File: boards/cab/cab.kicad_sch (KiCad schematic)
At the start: 0 parts

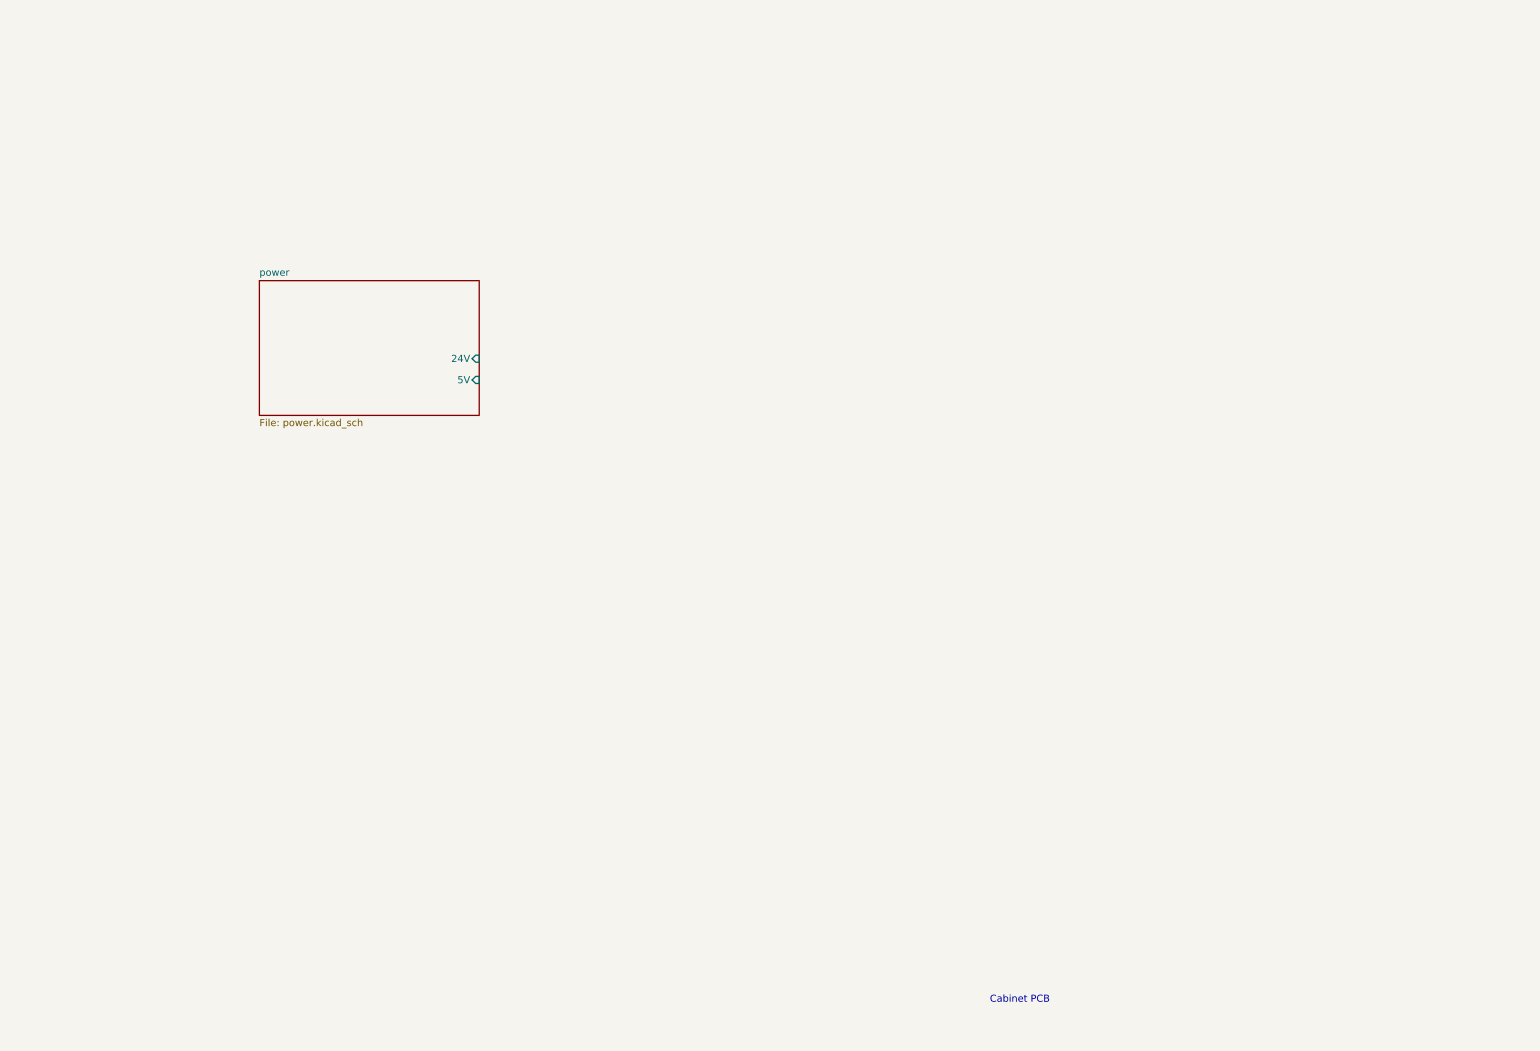
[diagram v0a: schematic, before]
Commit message: Removed hierarchy and added Connectors, Leds
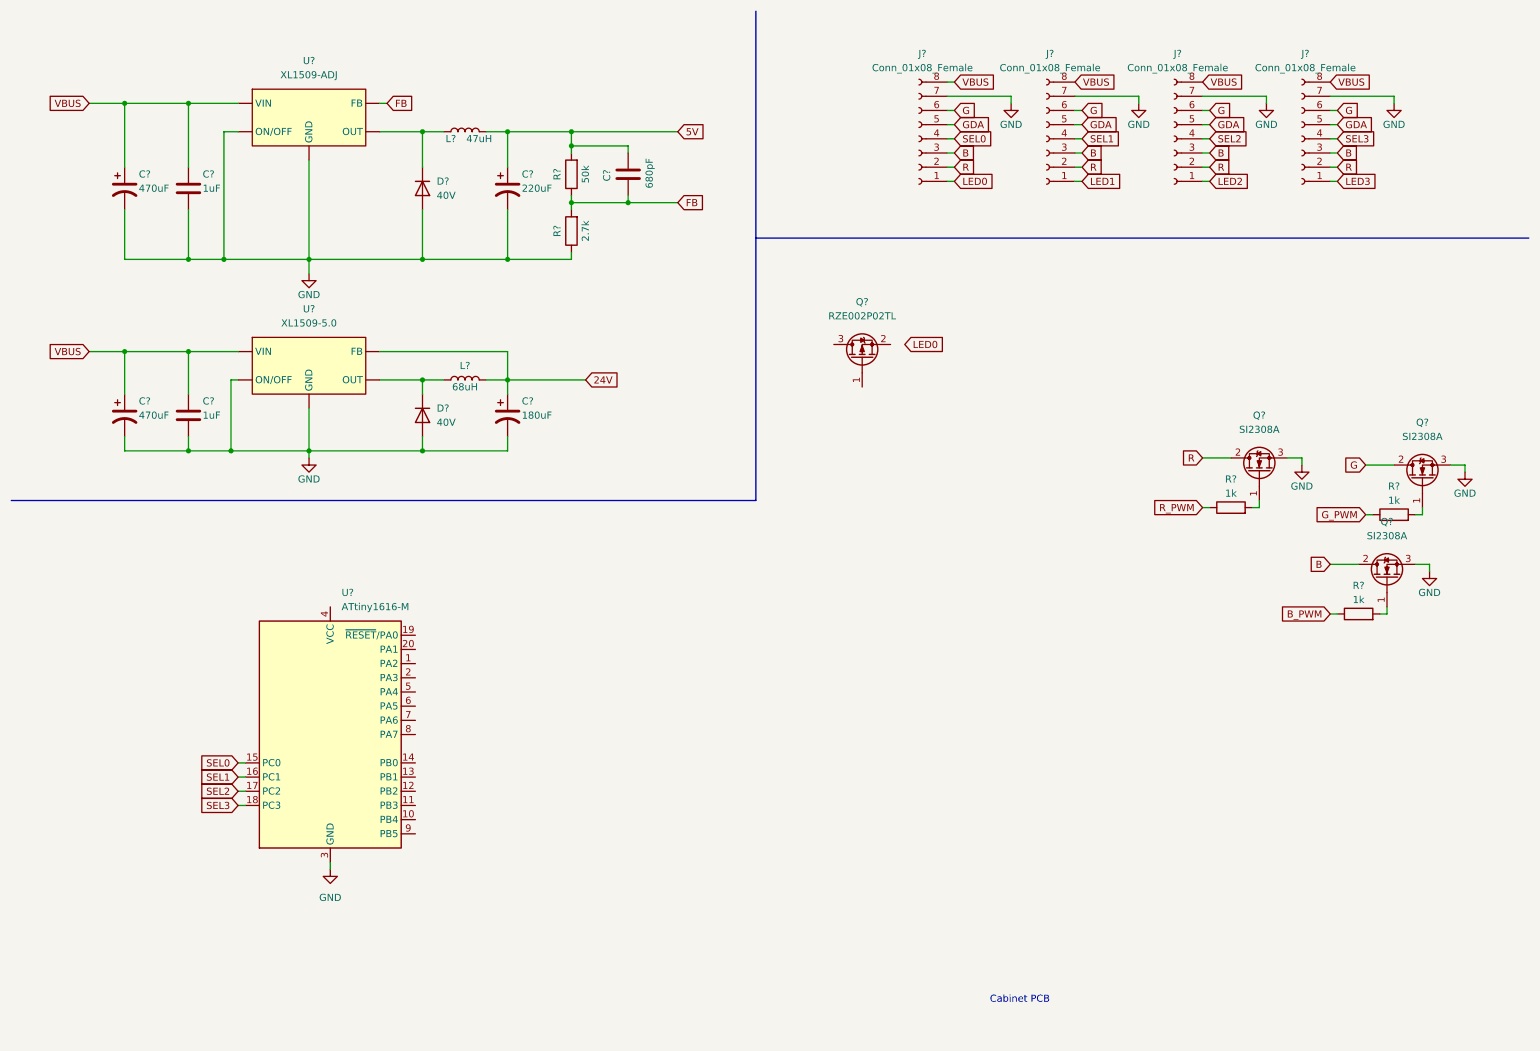
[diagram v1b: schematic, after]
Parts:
- added C?: 680pF, symbol Device:C
- added C? (x2): 470uF, symbol Device:C_Polarized_US
- added C? (x2): 1uF, symbol Device:C
- added C?: 180uF, symbol Device:C_Polarized_US
- added C?: 220uF, symbol Device:C_Polarized_US
- added D? (x2): 40V, symbol Device:D
- added J? (x4): Conn_01x08_Female, symbol Connector:Conn_01x08_Female
- added L?: 68uH, symbol Device:L
- added L?: 47uH, symbol Device:L
- added Q? (x3): SI2308A, Package_TO_SOT_SMD:TO-252-2, symbol Transistor_FET:STD7NK40Z
- added Q?: RZE002P02TL, symbol Transistor_FET:BSS84
- added R? (x3): 1k, symbol Device:R
- added R?: 50k, symbol Device:R
- added R?: 2.7k, symbol Device:R
- added U?: ATtiny1616-M, Package_DFN_QFN:VQFN-20-1EP_3x3mm_P0.4mm_EP1.7x1.7mm, symbol MCU_Microchip_ATtiny:ATtiny1616-M
- added U?: XL1509-ADJ, symbol StackCabinet:XL1509-ADJ
- added U?: XL1509-5.0, symbol StackCabinet:XL1509-5.0
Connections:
- new net: Q?.1 (G), R?.2 (x3)
- new net: D?.1 (K), L?.1, U?. (VIN) (x2)
- new net 24V: C?.1, L?.2, U?. (VIN)
- new net 5V: C?.1, C?.1, L?.2, R?.2
- new net B: J?.3 (Pin_3), J?.3 (Pin_3), J?.3 (Pin_3), J?.3 (Pin_3), Q?.2 (D)
- new net B_PWM: R?.1
- new net FB: C?.2, R?.1, R?.2, U?. (VIN)
- new net G: J?.6 (Pin_6), J?.6 (Pin_6), J?.6 (Pin_6), J?.6 (Pin_6), Q?.2 (D)
- new net GDA: J?.5 (Pin_5), J?.5 (Pin_5), J?.5 (Pin_5), J?.5 (Pin_5)
- new net GND: C?.2, C?.2, C?.2, C?.2, C?.2, C?.2, D?.2 (A), D?.2 (A), J?.7 (Pin_7), J?.7 (Pin_7), J?.7 (Pin_7), J?.7 (Pin_7), Q?.3 (S), Q?.3 (S), Q?.3 (S), R?.1, U?. (VIN), U?. (VIN), U?.21 (GND), U?.3 (GND)
- new net G_PWM: R?.1
- new net LED0: J?.1 (Pin_1)
- new net LED1: J?.1 (Pin_1)
- new net LED2: J?.1 (Pin_1)
- new net LED3: J?.1 (Pin_1)
- new net R: J?.2 (Pin_2), J?.2 (Pin_2), J?.2 (Pin_2), J?.2 (Pin_2), Q?.2 (D)
- new net R_PWM: R?.1
- new net SEL0: J?.4 (Pin_4), U?.15 (PC0)
- new net SEL1: J?.4 (Pin_4), U?.16 (PC1)
- new net SEL2: J?.4 (Pin_4), U?.17 (PC2)
- new net SEL3: J?.4 (Pin_4), U?.18 (PC3)
- new net VBUS: C?.1, C?.1, C?.1, C?.1, J?.8 (Pin_8), J?.8 (Pin_8), J?.8 (Pin_8), J?.8 (Pin_8), U?. (VIN), U?. (VIN)
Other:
- removed sheet power

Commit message: PCB
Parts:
- added C8, C9: 1uF, symbol Device:C
- added D3: 40V, symbol Device:D
- added L3: Solenoid, symbol Device:L
- added Q1: SI2308A, Package_TO_SOT_SMD:TO-252-2, symbol Transistor_FET:STD7NK40Z
- added Q4, Q6, Q8: RZE002P02TL, symbol Transistor_FET:BSS84
- gave numbers to parts that had none: 27
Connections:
- net 24V: now also D3.1 (K), L3.1
- net 5V: now also Q2.3 (D), U3.4 (VCC), C8.1, Q4.3 (D), Q6.3 (D), Q8.3 (D)
- net B_PWM: now also U3.5 (PA4)
- net GND: now also C8.2, C9.2, Q1.3 (S)
- net G_PWM: now also U3.2 (PA3)
- net LED0: now also Q2.2 (S)
- net LED1: now also Q4.2 (S)
- net LED2: now also Q6.2 (S)
- net LED3: now also Q8.2 (S)
- net R_PWM: now also U3.1 (PA2)
- net LED0_PWM: now reaches Q2.1 (G)
- net SOL_EN: now reaches U3.14 (PB0)
- net SOL_EN: now also Q1.1 (G)
- net LED1_PWM: now reaches U3.6 (PA5)
- net LED1_PWM: now also Q4.1 (G)
- net LED2_PWM: now reaches U3.7 (PA6)
- net LED2_PWM: now also Q6.1 (G)
- net LED3_PWM: now reaches U3.8 (PA7)
- net LED3_PWM: now also Q8.1 (G)
- new net: D3.2 (A), L3.2, Q1.2 (D)
- new net 24: C9.1
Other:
- note added: "Attiny1616"
- note added: "Connectors"
- note added: "LEDS"
- note added: "Power"
- note added: "Solenoid"
- moved on the sheet: C2, C4, C6, D2, L2, Q2, Q3, Q5, Q7, R3, R4, R5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
